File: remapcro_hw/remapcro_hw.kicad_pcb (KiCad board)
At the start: 2 copper layers, 33 parts, among them P1 CONN_01X10, P2 CONN_01X10, SW1 SW_PUSH_SMALL_H, SW10 SW_PUSH_SMALL_H, SW11 SW_PUSH_SMALL_H, SW12 SW_PUSH_SMALL_H, SW2 SW_PUSH_SMALL_H, SW3 SW_PUSH_SMALL_H, SW4 SW_PUSH_SMALL_H, SW5 SW_PUSH_SMALL_H, SW6 SW_PUSH_SMALL_H, SW7 SW_PUSH_SMALL_H, SW8 SW_PUSH_SMALL_H, SW9 SW_PUSH_SMALL_H, U1 LEO_PRO_MICRO, U2 IS25LQ, U3 USB_HOST_SHIELD_MINI

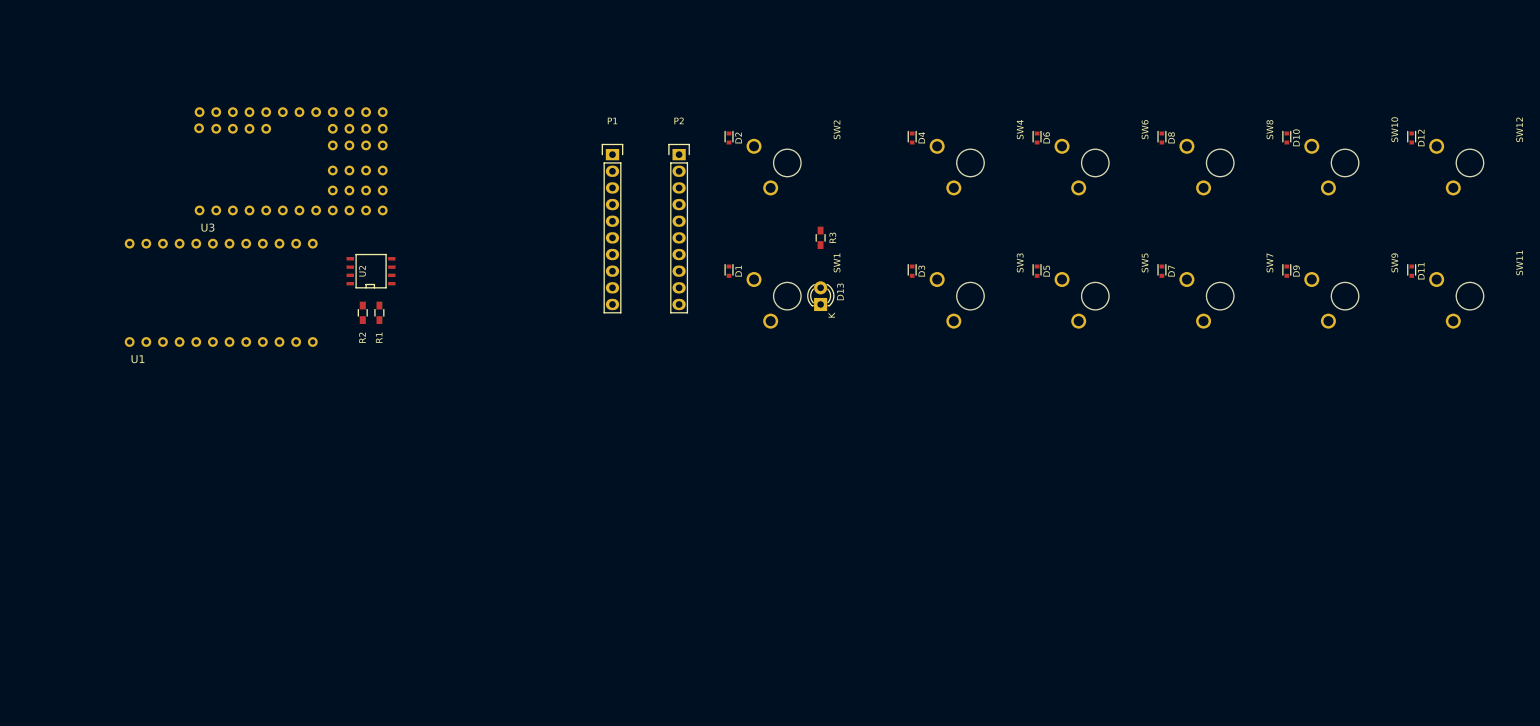
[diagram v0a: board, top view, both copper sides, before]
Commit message: rst switch, pcb layout
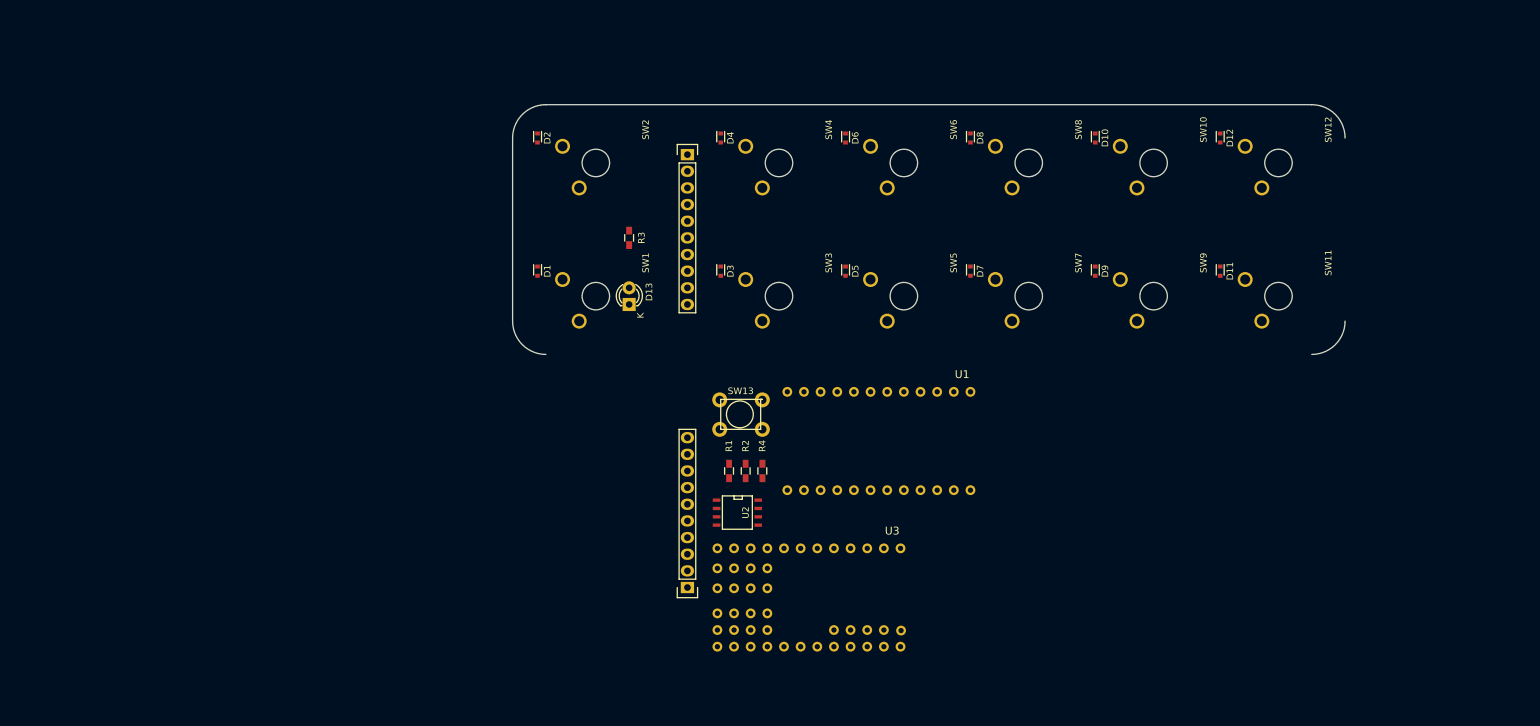
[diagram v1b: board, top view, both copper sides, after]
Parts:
- added R4: 4k7, Resistors_SMD:R_0603_HandSoldering, F.Cu at (127.0, 82.5)
- added SW13: SW_PUSH, components:SW_TACTILE_THT, F.Cu at (127.0, 76.2)
- moved U3 103.3 mm to (134.1, 101.9), turned to 180 degrees
- moved U1 102.8 mm to (144.8, 78.0), turned to 180 degrees
- moved P1 67.0 mm to (115.6, 100.3), turned to 180 degrees
- moved U2 66.9 mm to (123.2, 88.9), turned to 270 degrees
- moved R2 63.2 mm to (124.5, 82.5), turned to 270 degrees
- moved R1 58.5 mm to (121.9, 82.5), turned to 270 degrees
- moved D1 29.2 mm to (92.7, 52.1)
- moved D11 29.2 mm to (196.8, 52.1)
- moved D12 29.2 mm to (196.8, 31.8)
- moved D2 29.2 mm to (92.7, 31.8)
- moved D3 29.2 mm to (120.7, 52.1)
- moved D4 29.2 mm to (120.7, 31.8)
- moved D5 29.2 mm to (139.7, 52.1)
- moved D6 29.2 mm to (139.7, 31.8)
- moved D7 29.2 mm to (158.8, 52.1)
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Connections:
- net /R2 renamed /kR2
- D1 pad 1: /R1 -> /kR1
- D11 pad 1: /R3 -> /kR3
- D12 pad 1: /R3 -> /kR3
- D13 pad 1: /LED_MACRO -> /kLED_MACRO
- D2 pad 1: /R1 -> /kR1
- D5 pad 1: /R3 -> /kR3
- D6 pad 1: /R3 -> /kR3
- D7 pad 1: /R1 -> /kR1
- D8 pad 1: /R1 -> /kR1
- P1 pad 2: /C0 -> (no net)
- P1 pad 3: /C1 -> (no net)
- P1 pad 4: /C2 -> (no net)
- P1 pad 5: /C3 -> (no net)
- P1 pad 6: /R0 -> (no net)
- P1 pad 7: /R1 -> (no net)
- P1 pad 8: /R3 -> (no net)
- P2 pad 1: +3V3 -> GND
- P2 pad 10: GND -> +3V3
- P2 pad 2: /C0 -> /kLED_MACRO
- P2 pad 3: /C1 -> /kR3
- P2 pad 4: /C2 -> /kR1
- P2 pad 5: /C3 -> (no net)
- P2 pad 6: /R0 -> /kC3
- P2 pad 7: /R1 -> (no net)
- P2 pad 8: /R3 -> /kC1
- P2 pad 9: /LED_MACRO -> /kC0
- SW1 pad 1: /C0 -> /kC0
- SW10 pad 1: /C3 -> /kC3
- SW11 pad 1: /C1 -> /kC1
- SW12 pad 1: /C3 -> /kC3
- SW2 pad 1: /C1 -> /kC1
- SW3 pad 1: /C0 -> /kC0
- SW4 pad 1: /C1 -> /kC1
- SW5 pad 1: /C0 -> /kC0
- SW6 pad 1: /C1 -> /kC1
- SW7 pad 1: /C1 -> /kC1
- SW8 pad 1: /C3 -> /kC3
- SW9 pad 1: /C1 -> /kC1
- U1 pad 21: (no net) -> /RST
- U3 pad 22: (no net) -> /RST
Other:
- board outline added: 127 x 38.1 mm

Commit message: more pcb layout
probably fab as two separate boards!
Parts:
- SW13: moved to B.Cu
- moved U1 104.3 mm to (41.9, 95.2), turned to 0 degrees
- moved U3 85.7 mm to (52.7, 74.9), turned to 0 degrees
- moved R4 68.4 mm to (59.7, 94.6), turned to 90 degrees
- moved D6 63.6 mm to (76.2, 29.2)
- moved D10 63.5 mm to (114.3, 30.5)
- moved D9 63.5 mm to (114.3, 50.8)
- moved D13 63.5 mm to (43.2, 55.9)
- moved D3 63.5 mm to (57.1, 50.8)
- moved D4 63.5 mm to (57.1, 30.5)
- moved R3 63.5 mm to (43.2, 45.7)
- moved D11 63.5 mm to (133.3, 50.8)
- moved D12 63.5 mm to (133.3, 30.5)
- moved D7 63.5 mm to (95.2, 50.8)
- moved D8 63.5 mm to (95.2, 30.5)
- moved SW10 63.5 mm to (123.2, 34.3)
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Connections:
- D1 pad 1: /kR1 -> /kR0
- D10 pad 1: /kR2 -> /kR1
- D11 pad 1: /kR3 -> /kR2
- D12 pad 1: /kR3 -> /kR2
- D2 pad 1: /kR1 -> /kR0
- D3 pad 1: /kR2 -> /kR1
- D4 pad 1: /kR2 -> /kR1
- D5 pad 1: /kR3 -> /kR2
- D6 pad 1: /kR3 -> /kR2
- D7 pad 1: /kR1 -> /kR0
- D8 pad 1: /kR1 -> /kR0
- D9 pad 1: /kR2 -> /kR1
- P1 pad 2: (no net) -> /GO0
- P1 pad 3: (no net) -> /GO1
- P1 pad 4: (no net) -> /GO2
- P1 pad 5: (no net) -> /GO3
- P1 pad 6: (no net) -> /GI0
- P1 pad 7: (no net) -> /GI1
- P1 pad 8: (no net) -> /GI2
- P2 pad 1: GND -> +3V3
- P2 pad 10: +3V3 -> GND
- P2 pad 2: /kLED_MACRO -> /kC0
- P2 pad 3: /kR3 -> /kC1
- P2 pad 4: /kR1 -> /kC2
- P2 pad 5: (no net) -> /kC3
- P2 pad 6: /kC3 -> /kR0
- P2 pad 7: (no net) -> /kR1
- P2 pad 8: /kC1 -> /kR2
- P2 pad 9: /kC0 -> /kLED_MACRO
- SW2 pad 1: /kC1 -> /kC2
- SW4 pad 1: /kC1 -> /kC2
- SW6 pad 1: /kC1 -> /kC2
- U1 pad 20: +3V3 -> (no net)
- U1 pad 21: /RST -> +3V3
- U1 pad 22: (no net) -> /RST
- U3 pad 30: (no net) -> /GI0
- U3 pad 31: (no net) -> /GI1
- U3 pad 32: (no net) -> /GI2
- U3 pad 38: (no net) -> /GO0
- U3 pad 39: (no net) -> /GO1
- U3 pad 4: (no net) -> /SCK
- U3 pad 40: (no net) -> /GO2
- U3 pad 41: (no net) -> /GO3
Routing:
- net +3V3: track 0.00 -> 138.9 mm, vias 0 -> 3
- net GND: track 0.00 -> 137.8 mm, vias 0 -> 2
- net /kR0: track 0.00 -> 134.6 mm, vias 0 -> 3
- net /kR2: track 0.00 -> 126.4 mm, vias 0 -> 2
- net /kR1: track 0.00 -> 123.5 mm, vias 0 -> 2
- net /RST: track 0.00 -> 114.9 mm
- net /kC0: track 0.00 -> 110.4 mm, vias 0 -> 1
- net /kC1: track 0.00 -> 80.3 mm, vias 0 -> 1
- net /kC3: track 0.00 -> 69.1 mm, vias 0 -> 1
- net /kC2: track 0.00 -> 49.1 mm
- net /LED_MACRO: track 0.00 -> 41.1 mm
- net /MISO: track 0.00 -> 38.0 mm, vias 0 -> 1
- net /kLED_MACRO: track 0.00 -> 34.9 mm
- net /FLASH_SS: track 0.00 -> 32.4 mm, vias 0 -> 2
- net /MOSI: track 0.00 -> 29.1 mm
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- added copper zone on B.Cu, net GND
- added copper zone on F.Cu, net GND
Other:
- board size 127 x 38.1 mm -> 127 x 78.7 mm

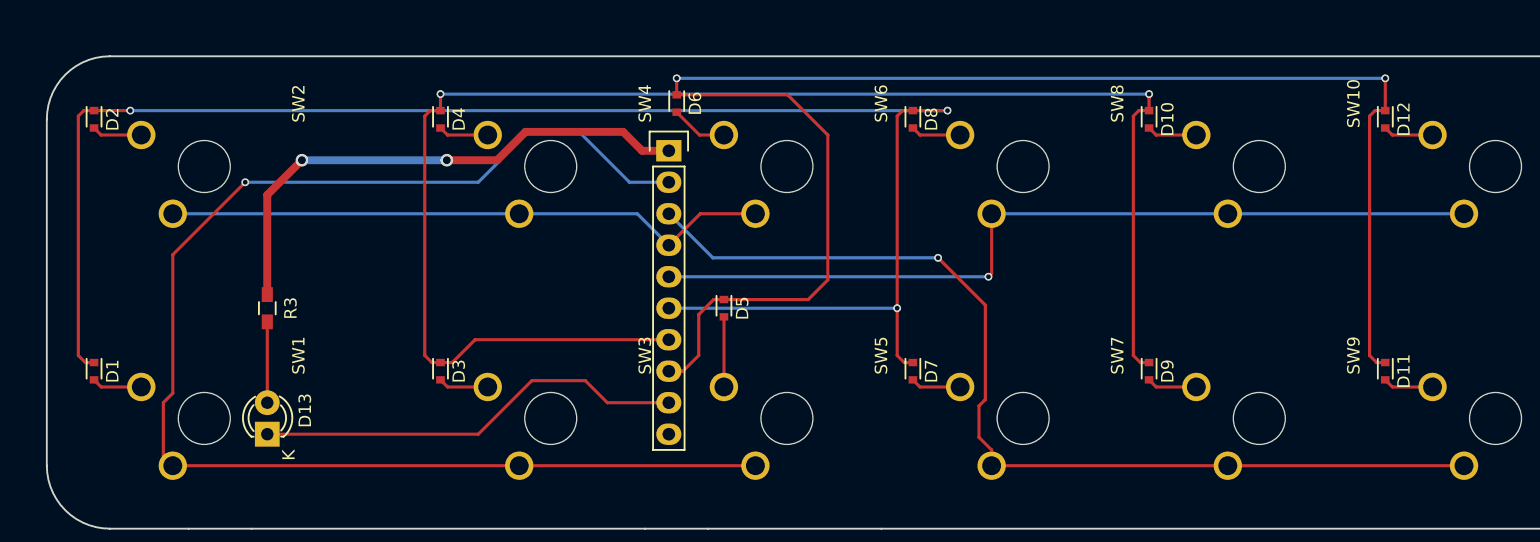
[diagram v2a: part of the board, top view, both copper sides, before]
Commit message: tweaks including hand-solderable SMD diode
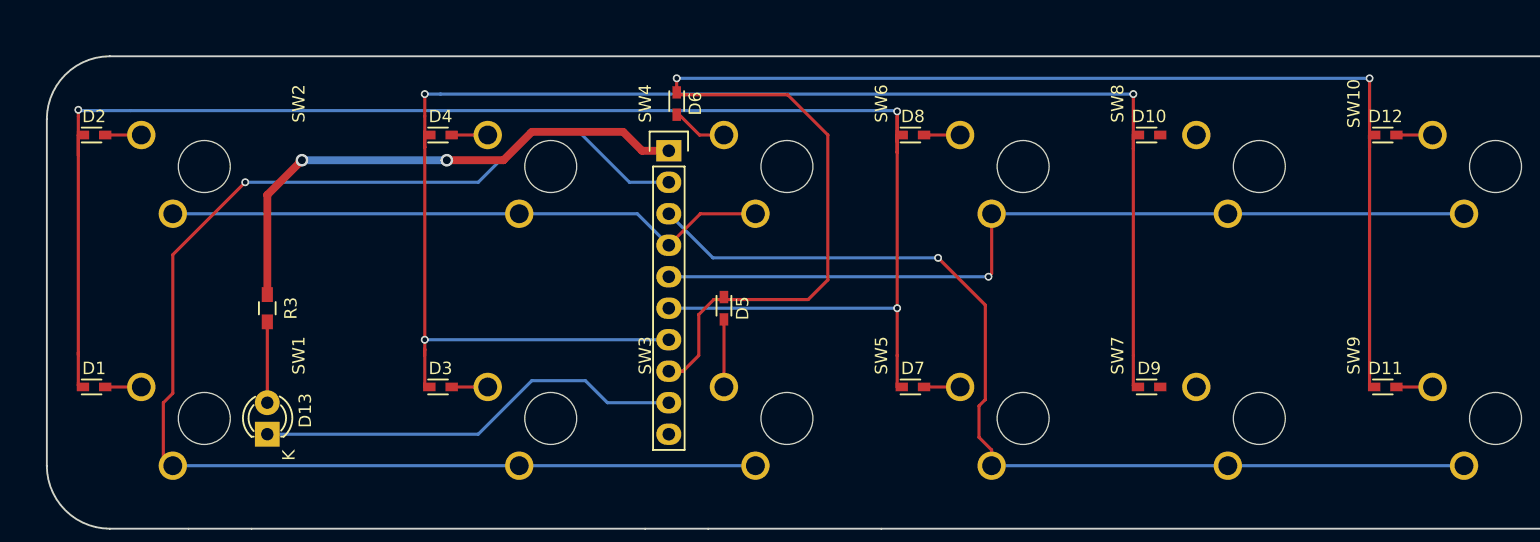
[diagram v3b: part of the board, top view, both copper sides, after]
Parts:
- D1, D10, D11, D12, D2, D3, D4, D5, D6, D7, D8, D9: footprint Diodes_SMD:SOD-523 -> components:SOD-523-handsoldering
- moved D1 1.27 mm to (29.2, 52.1), turned to 0 degrees
- moved D11 1.27 mm to (133.3, 52.1), turned to 0 degrees
- moved D3 1.27 mm to (57.1, 52.1), turned to 0 degrees
- moved D7 1.27 mm to (95.2, 52.1), turned to 0 degrees
- moved D9 1.27 mm to (114.3, 52.1), turned to 0 degrees
- moved D10 1.27 mm to (114.3, 31.8), turned to 0 degrees
- moved D12 1.27 mm to (133.3, 31.8), turned to 0 degrees
- moved D2 1.27 mm to (29.2, 31.8), turned to 0 degrees
- moved D4 1.27 mm to (57.1, 31.8), turned to 0 degrees
- moved D8 1.27 mm to (95.2, 31.8), turned to 0 degrees
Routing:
- net /kR1: track 123.5 -> 128.2 mm, vias 2 -> 3
- net Net-(D9-Pad2): track 4.05 -> 0.00 mm
- net Net-(D10-Pad2): track 4.05 -> 0.00 mm
- net /kR0: track 134.6 -> 136.0 mm
- net Net-(D8-Pad2): track 4.05 -> 2.91 mm
- net Net-(D7-Pad2): track 4.05 -> 2.91 mm
- net Net-(D12-Pad2): track 4.05 -> 2.91 mm
- net Net-(D11-Pad2): track 4.05 -> 2.91 mm
- net Net-(D4-Pad2): track 4.05 -> 2.91 mm
- net Net-(D3-Pad2): track 4.05 -> 2.91 mm
- net Net-(D2-Pad2): track 4.05 -> 2.91 mm
- net Net-(D1-Pad2): track 4.05 -> 2.91 mm
- net /kR2: track 126.4 -> 126.9 mm
